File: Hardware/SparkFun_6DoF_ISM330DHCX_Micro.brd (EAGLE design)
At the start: 20.3 x 12.7 mm, 60 parts, among them U1 ISM330DHCX

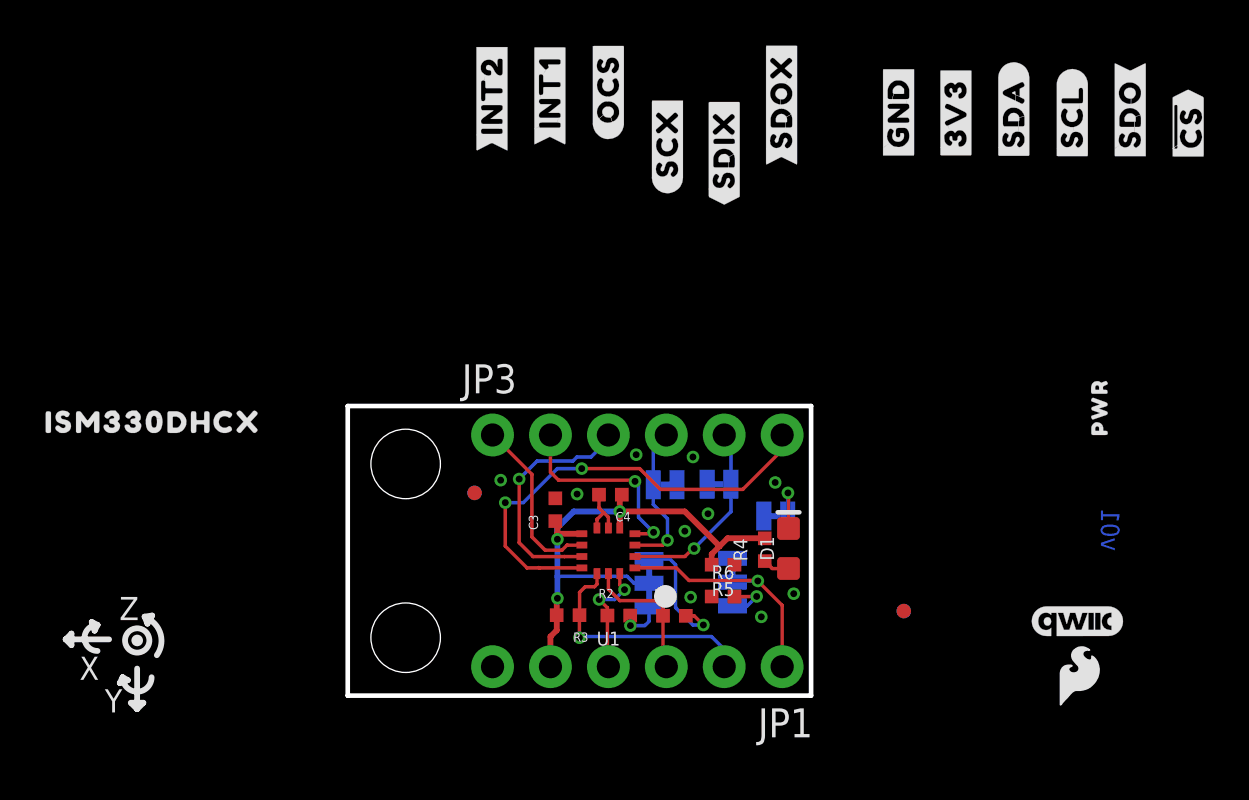
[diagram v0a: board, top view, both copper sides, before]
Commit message: Moves the i2c jumper
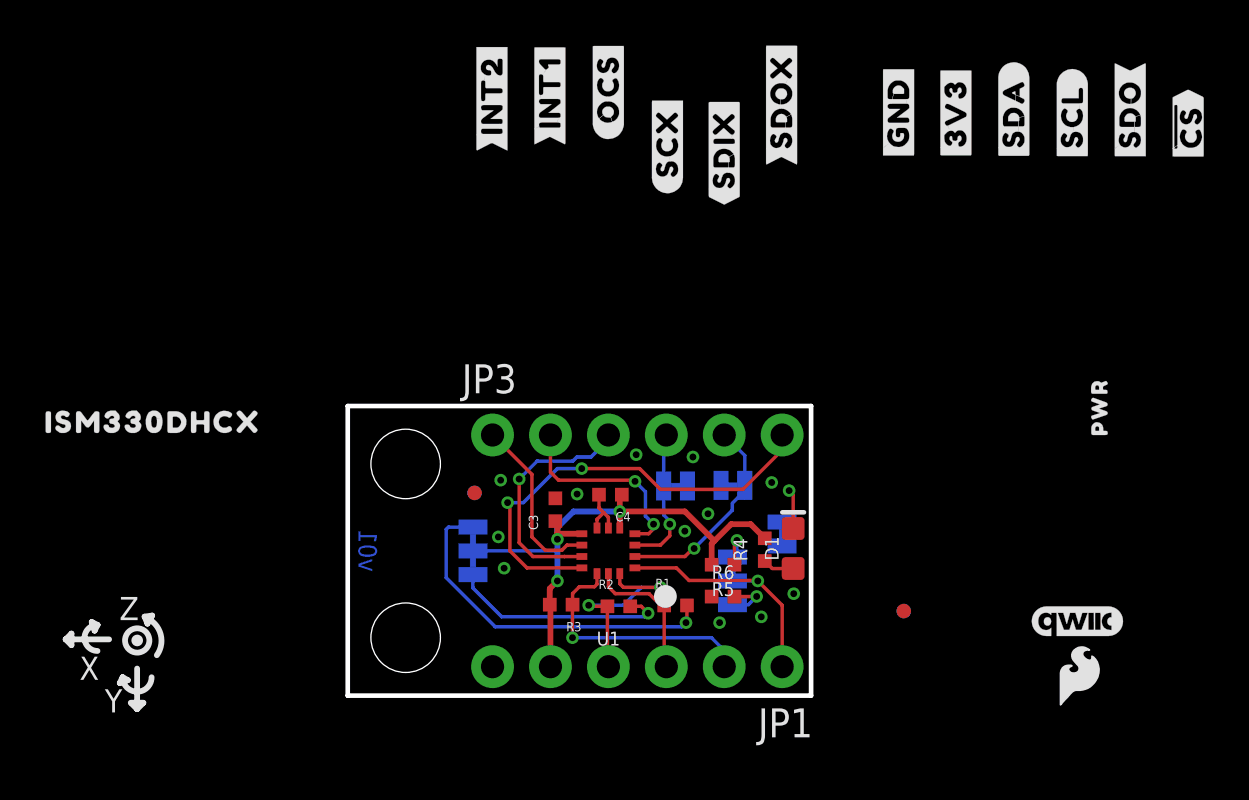
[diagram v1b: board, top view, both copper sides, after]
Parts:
- moved U$14 10.5 mm to (23.4, 11.5)
- moved U$13 10.3 mm to (23.1, 10.3)
- moved I2C_PU 7.85 mm to (5.49, 11.4)
- moved LED 0.84 mm to (19.1, 12.2), turned to 90 degrees
- moved SDX 0.61 mm to (16.9, 14.3)
- moved R3 0.55 mm to (9.36, 9.07)
- moved R1 0.46 mm to (14.4, 9.04)
- moved SCX 0.46 mm to (14.4, 14.3)
- moved R2 0.41 mm to (11.9, 9.00)
- moved D1 0.20 mm to (19.5, 11.5)
- moved ADDR 0.05 mm to (16.9, 10.1)
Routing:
- net N$5: track 5.64 -> 15.6 mm
- net N$6: track 1.97 -> 9.77 mm
- net SDA: track 5.20 -> 9.27 mm
- net N$1: track 0.00 -> 1.93 mm, vias 0 -> 1
- net N$3: track 2.59 -> 1.74 mm
- net SDI_AUX: track 8.51 -> 9.19 mm
- net !CS!: track 10.7 -> 11.2 mm
- net GND: vias 10 -> 12

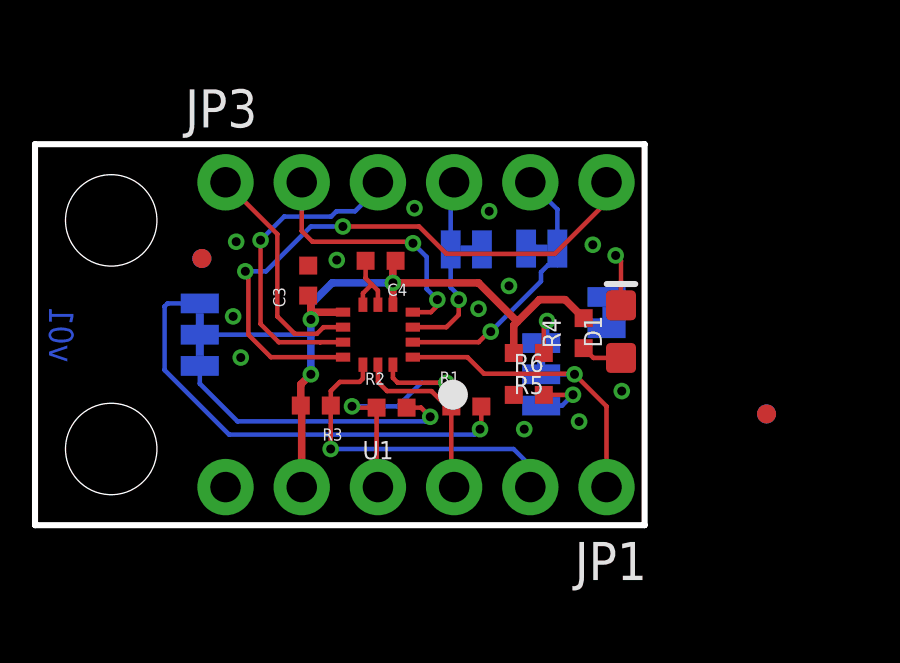
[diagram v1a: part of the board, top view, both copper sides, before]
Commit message: Moves SDI_Aux and SDO_Aux jumpers to topside
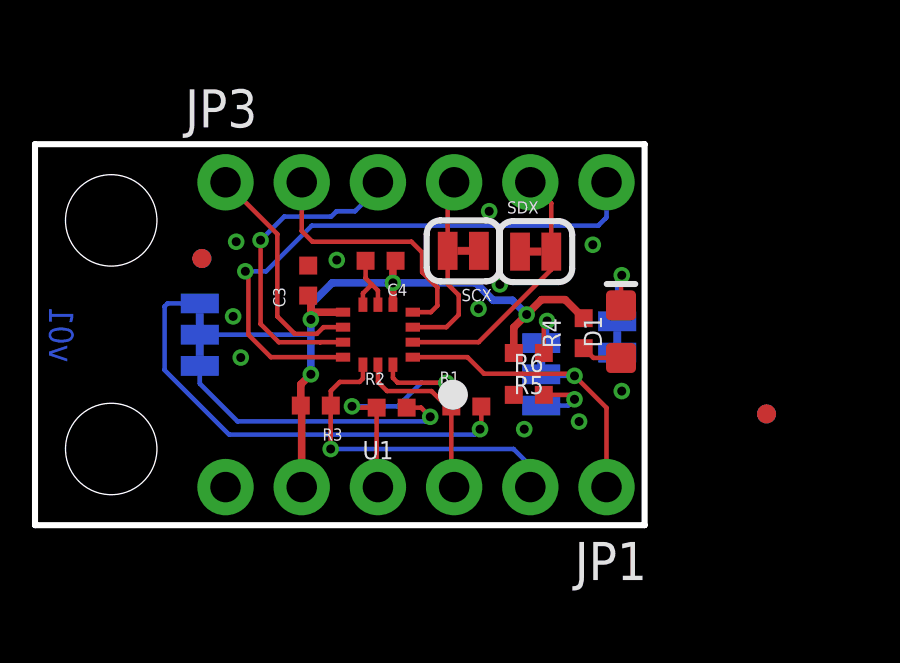
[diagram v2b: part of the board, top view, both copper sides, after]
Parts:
- moved LED 0.89 mm to (19.4, 11.4)
- moved SDX 0.23 mm to (16.7, 14.2), flipped to the top, turned to 0 degrees
- moved SCX 0.11 mm to (14.3, 14.2), flipped to the top, turned to 180 degrees
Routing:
- net N$3: track 1.74 -> 2.61 mm
- net SDO_AUX: track 20.0 -> 19.6 mm, vias 2 -> 1
- net SDI_AUX: track 9.19 -> 8.82 mm, vias 1 -> 0
- net 3.3V: track 24.9 -> 25.1 mm, vias 3 -> 4
- net SCX: track 6.28 -> 6.36 mm, vias 1 -> 0
- net INT1: vias 2 -> 0
- net GND: vias 12 -> 11

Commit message: Moves fiducials back, cleans up some traces
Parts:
- moved FD2 6.73 mm to (17.8, 7.47)
- moved FID2 6.73 mm to (17.8, 7.47)
- moved C4 0.10 mm to (11.4, 13.9)
- moved C3 0.05 mm to (9.11, 13.3)
- moved LED 0.05 mm to (19.4, 11.4)
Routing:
- net GND: track 2.43 -> 4.21 mm, vias 11 -> 12
- net INT1: track 8.83 -> 8.25 mm
- net SCX: track 6.36 -> 5.84 mm

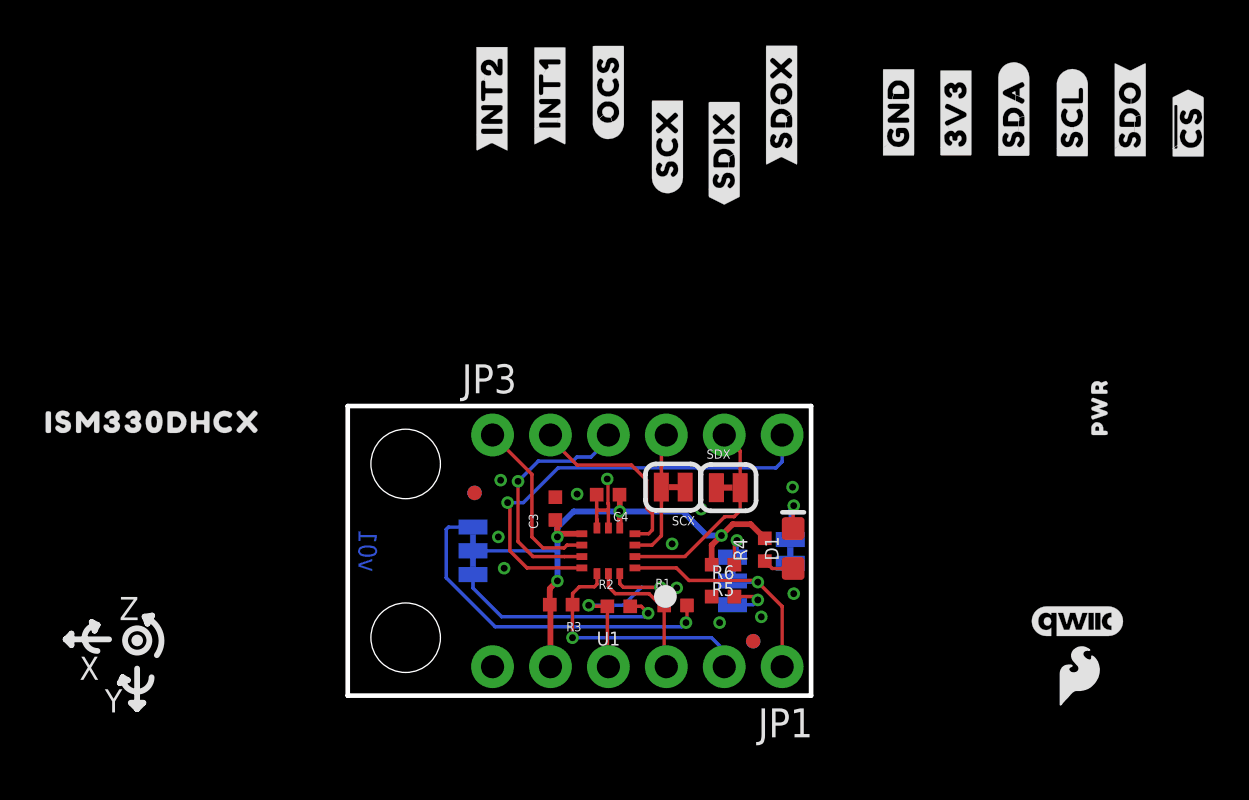
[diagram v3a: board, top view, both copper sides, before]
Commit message: Adds labels to Mini
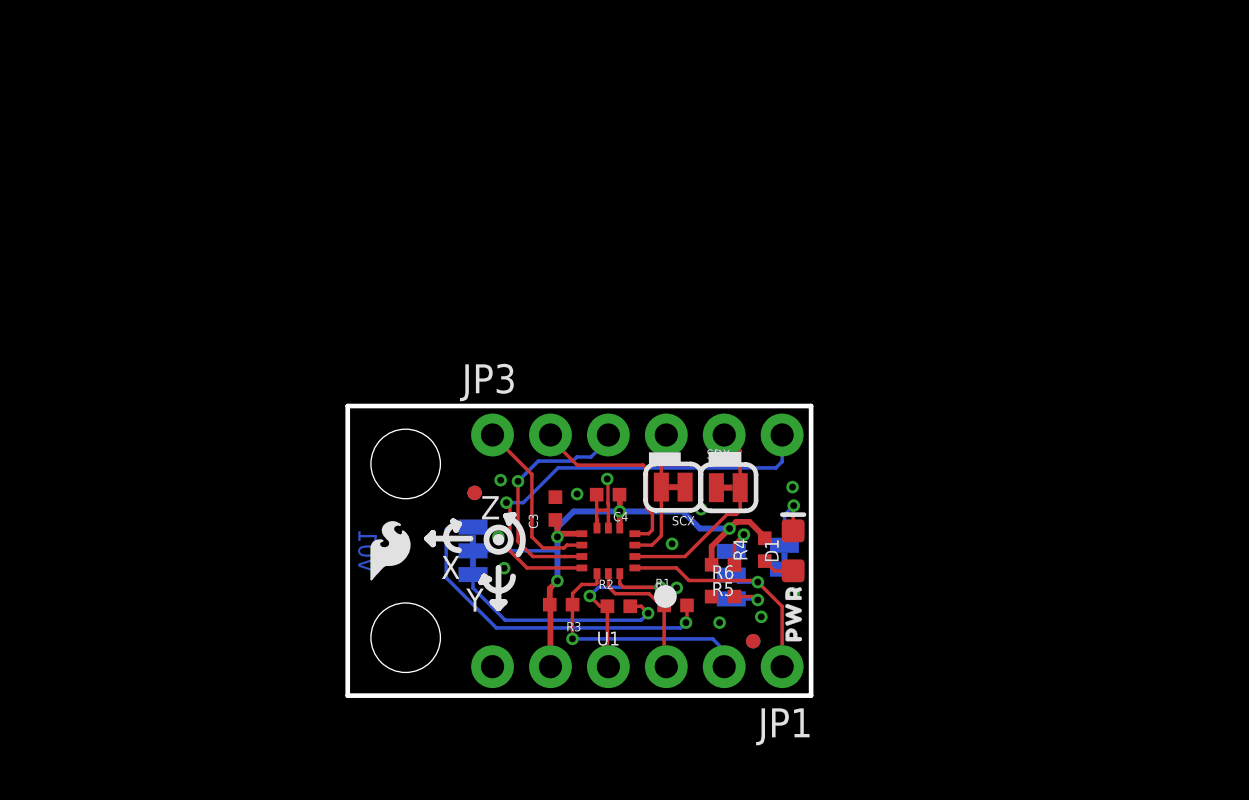
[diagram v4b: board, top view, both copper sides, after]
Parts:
- removed LOGO1: QWIIC_LOGO_4MM, SparkFun-Aesthetics:QWIIC_4MM
- removed LOGO3: SFE_LOGO_NAME_FLAME.1_INCH, SparkFun-Aesthetics:SFE_LOGO_NAME_FLAME_.1
- removed U$10: (no value), top:#SCX#9
- removed U$11: (no value), top:#SDIX#11
- removed U$12: (no value), ISMTop:ISM330DHCX331
- removed U$15: (no value), bot:#3V3#1
- removed U$17: (no value), bot:#GND#0
- removed U$18: (no value), bot:#SDO#7
- removed U$19: (no value), bot:#INT1#9
- removed U$20: (no value), bot:#OCS#7
- removed U$21: (no value), bot:#INT2#9
- removed U$22: (no value), bot:#SCL#5
- removed U$23: (no value), bot:#SCX#8
- removed U$24: (no value), top:#SDOX#12
- removed U$26: (no value), bot:#SDI#4
- removed U$27: (no value), bot:##CS##8
- removed U$3: (no value), top:##CS##7
- removed U$30: (no value), ISMTop:ISM330DHCX20
- removed U$31: (no value), top:6DOF12
- removed U$32: (no value), bot:#SDOX#12
- removed U$33: (no value), bot:#SDIX#11
- removed U$4: (no value), top:#SDA#4
- removed U$5: (no value), top:#SCL#5
- removed U$6: (no value), top:#SDO#6
- removed U$7: (no value), top:#INT1#9
- removed U$8: (no value), top:#INT2#9
- removed U$9: (no value), top:#OCS#8
- added U$34: (no value), ISMTopMini:SDOX9
- added U$35: (no value), ISMTopMini:SDIX8
- added U$36: (no value), ISMTopMini:SCX7
- added U$37: (no value), ISMTopMini:SCL5
- added U$38: (no value), ISMTopMini:#CS#2114
- added U$39: (no value), ISMTopMini:SDO2113
- added U$40: (no value), ISMTopMini:SDA6
- added U$41: (no value), ISMTopMini:3V30
- added U$42: (no value), ISMTopMini:GND4
- added U$43: (no value), ISMTopMini:OCS2112
- added U$44: (no value), ISMTopMini:INT110
- added U$45: (no value), ISMTopMini:INT2111
- U$1: device top:#3V3#1 -> ISMTopMini:ISM330DHCX2115
- U$2: device top:#GND#0 -> ISMTopMini:6DOF2115
- moved U$29 30.7 mm to (1.85, 11.5)
- moved LOGO2 29.6 mm to (1.83, 11.5)
- moved U$1 25.4 mm to (10.1, 11.4), flipped to the bottom, turned to 270 degrees
- moved U$2 25.3 mm to (7.77, 11.4), flipped to the bottom, turned to 270 degrees
- moved U$16 17.7 mm to (14.1, 12.5)
- moved U$28 16.2 mm to (19.6, 8.69)
- moved U$14 9.15 mm to (14.2, 11.3)
- moved U$13 8.95 mm to (14.2, 9.98)
- moved U$25 2.84 mm to (3.89, 11.4)
- moved LED 0.36 mm to (19.2, 11.2)
- moved ADDR 0.26 mm to (16.8, 10.4)
- moved D1 0.10 mm to (19.5, 11.4)
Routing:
- net N$1: track 1.93 -> 2.46 mm
